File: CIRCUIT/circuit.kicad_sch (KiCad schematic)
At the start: 13 parts, among them Q1 FQP30N06L, SW1 POWER SWITCH

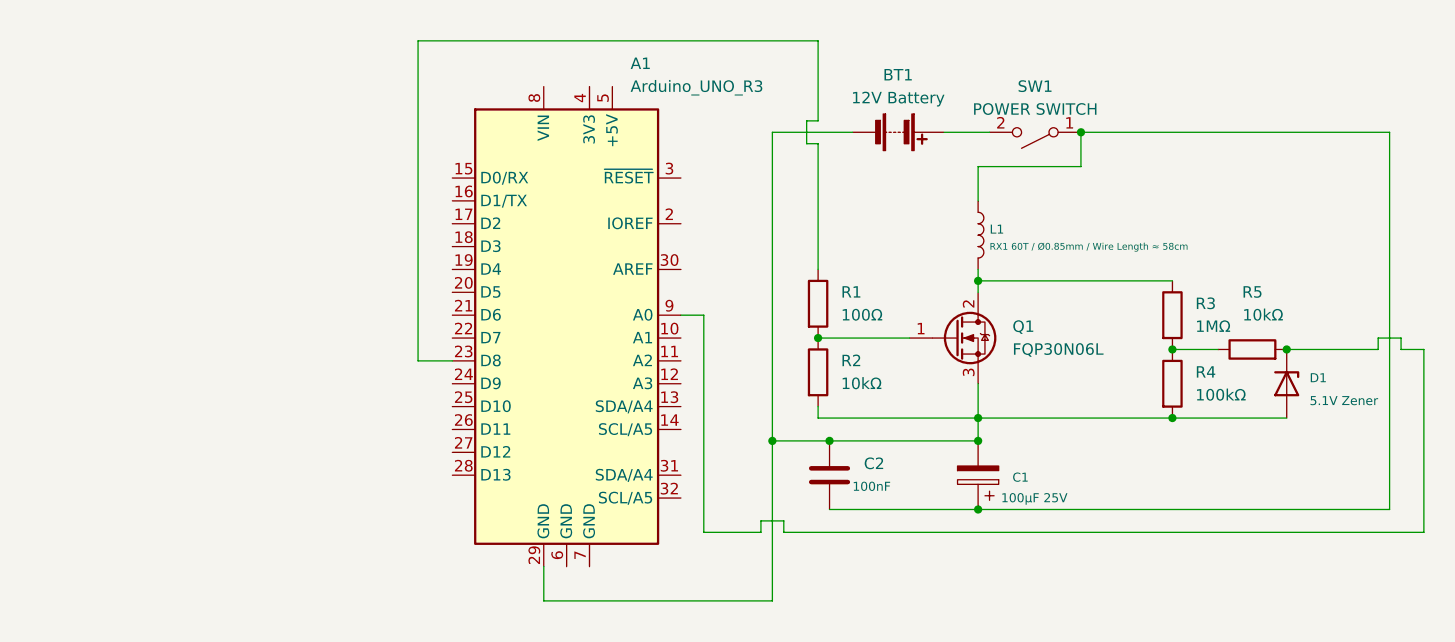
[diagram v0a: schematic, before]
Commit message: Add Op Amp To Circuit
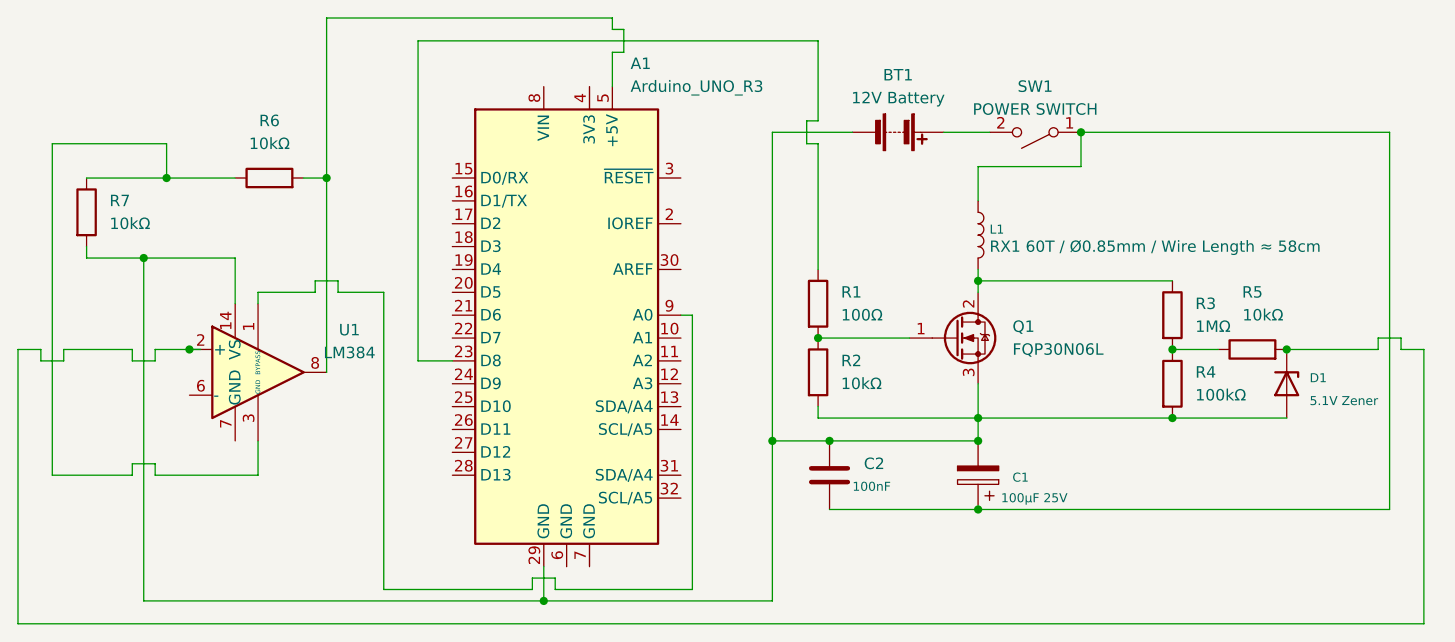
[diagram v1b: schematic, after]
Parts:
- added R6, R7: 10kΩ, symbol Device:R
- added U1: LM384, Package_DIP:DIP-14_W7.62mm, symbol Amplifier_Audio:LM384
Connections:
- net at A1.29 (GND), BT1.2 (-), C1.2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: now also R7.2, U1.14 (VS)
- net at A1.5 (+5V): now also R6.2, U1.8
- net at D1.1 (K), R5.2: now also U1.2 (+); no longer A1.9 (A0)
- new net: A1.9 (A0), U1.1 (BYPASS)
- new net: R6.1, R7.1, U1.10 (GND), U1.11 (GND), U1.12 (GND), U1.3 (GND), U1.4 (GND), U1.5 (GND)

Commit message: Add Resistor 50 k ohm
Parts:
- added R8: 50kΩ, symbol Device:R
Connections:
- net at A1.9 (A0), U1.1 (BYPASS): now also R8.2
- net at D1.1 (K), R5.2, U1.2 (+): now also R8.1
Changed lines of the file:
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@@
   (junction (at 133.35 93.98) (diameter 0) (color 0 0 0 0)
   )
+  (junction (at 53.34 80.01) (diameter 0) (color 0 0 0 0)
+  )
   (junction (at 60.96 67.31) (diameter 0) (color 0 0 0 0)
   )
@@
     (stroke (width 0) (type default) (color 0 0 0 0))
   )
+  (wire (pts (xy 45.72 74.93) (xy 44.45 74.93))
+    (stroke (width 0) (type default) (color 0 0 0 0))
+  )
   (wire (pts (xy 177.8 85.09) (xy 180.34 85.09))
     (stroke (width 0) (type default) (color 0 0 0 0))
@@
     (stroke (width 0) (type default) (color 0 0 0 0))
   )
+  (wire (pts (xy 44.45 77.47) (xy 45.72 77.47))
+    (stroke (width 0) (type default) (color 0 0 0 0))
+  )
+  (wire (pts (xy 45.72 77.47) (xy 45.72 86.36))
+    (stroke (width 0) (type default) (color 0 0 0 0))
+  )
   (wire (pts (xy 180.34 86.36) (xy 182.88 86.36))
     (stroke (width 0) (type default) (color 0 0 0 0))
@@
     (stroke (width 0) (type default) (color 0 0 0 0))
   )
+  (wire (pts (xy 44.45 74.93) (xy 44.45 77.47))
+    (stroke (width 0) (type default) (color 0 0 0 0))
+  )
   (wire (pts (xy 110.49 62.23) (xy 110.49 96.52))
     (stroke (width 0) (type default) (color 0 0 0 0))
@@
     (stroke (width 0) (type default) (color 0 0 0 0))
   )
+  (wire (pts (xy 45.72 73.66) (xy 45.72 74.93))
+    (stroke (width 0) (type default) (color 0 0 0 0))
+  )
   (wire (pts (xy 60.96 49.53) (xy 60.96 67.31))
     (stroke (width 0) (type default) (color 0 0 0 0))
@@
     (stroke (width 0) (type default) (color 0 0 0 0))
   )
+  (wire (pts (xy 53.34 73.66) (xy 53.34 80.01))
+    (stroke (width 0) (type default) (color 0 0 0 0))
+  )
   (wire (pts (xy 85.09 114.3) (xy 85.09 110.49))
     (stroke (width 0) (type default) (color 0 0 0 0))
@@
     )
     (property "Datasheet" "~" (id 3) (at 115.57 88.9 0)
+      (effects (font (size 1.27 1.27)) hide)
+    )
+    (pin "1")
+    (pin "2")
+  )
+  (symbol (lib_id "Device:R") (at 49.53 73.66 90) (unit 1)
+    (in_bom yes) (on_board yes)
+    (property "Reference" "R8" (id 0) (at 49.53 69 90)
+      (effects (font (size 1 1)))
+    )
+    (property "Value" "50kΩ" (id 1) (at 49 71.12 90)
+      (effects (font (size 1 1)))
+    )
+    (property "Footprint" "" (id 2) (at 49.53 75.438 90)
+      (effects (font (size 1.27 1.27)) hide)
+    )
+    (property "Datasheet" "~" (id 3) (at 49.53 73.66 0)
       (effects (font (size 1.27 1.27)) hide)
     )
@@
       (reference "R7") (unit 1) (value "10kΩ") (footprint "")
     )
+    (path "/3de27c1c-897a-4a6c-b0f7-6b3c6fd91fd1"
+      (reference "R8") (unit 1) (value "50kΩ") (footprint "")
+    )
     (path "/f88f566c-222e-406b-b3b8-75df684e7c33"
